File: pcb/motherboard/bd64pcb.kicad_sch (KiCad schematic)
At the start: 224 parts, among them J1 SM04B-SRSS-TB, J2 SM05B-SURS-TF, J3 SM05B-SURS-TF, SW1 SW_Push, U1 ATmega32U4-MU, U2 IS31FL3733-QF, Y1 16MHz

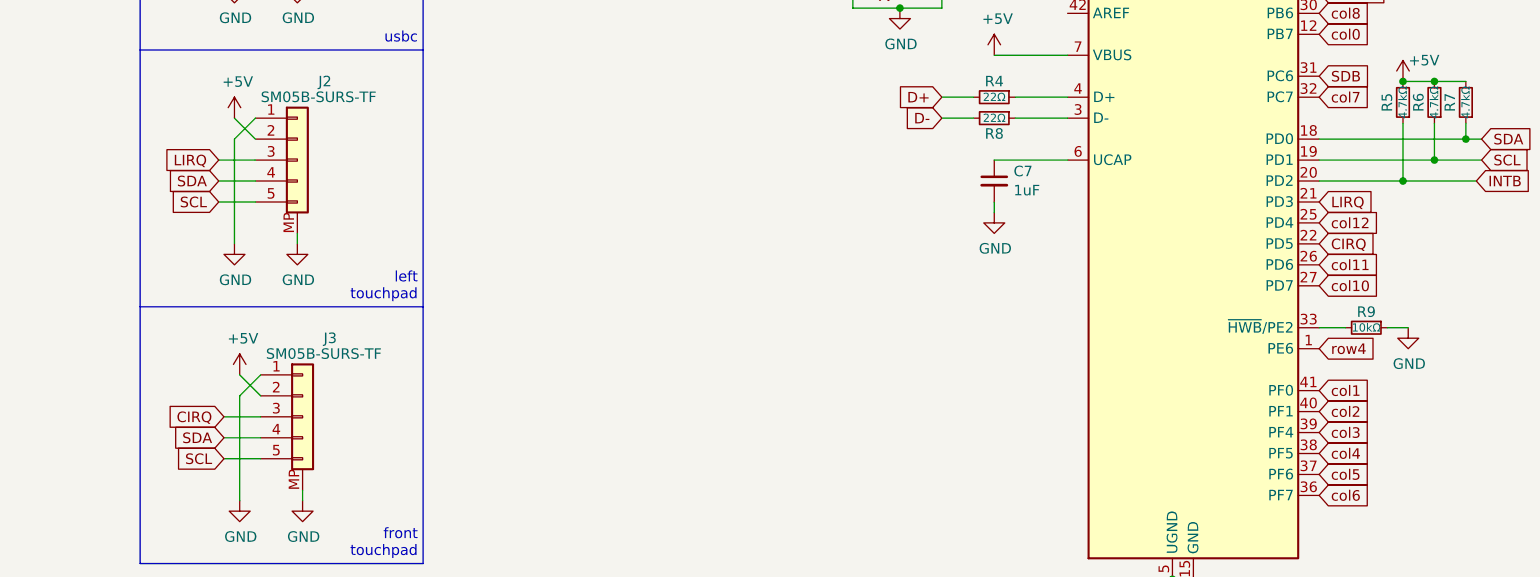
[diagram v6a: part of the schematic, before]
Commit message: IRQ > VIB
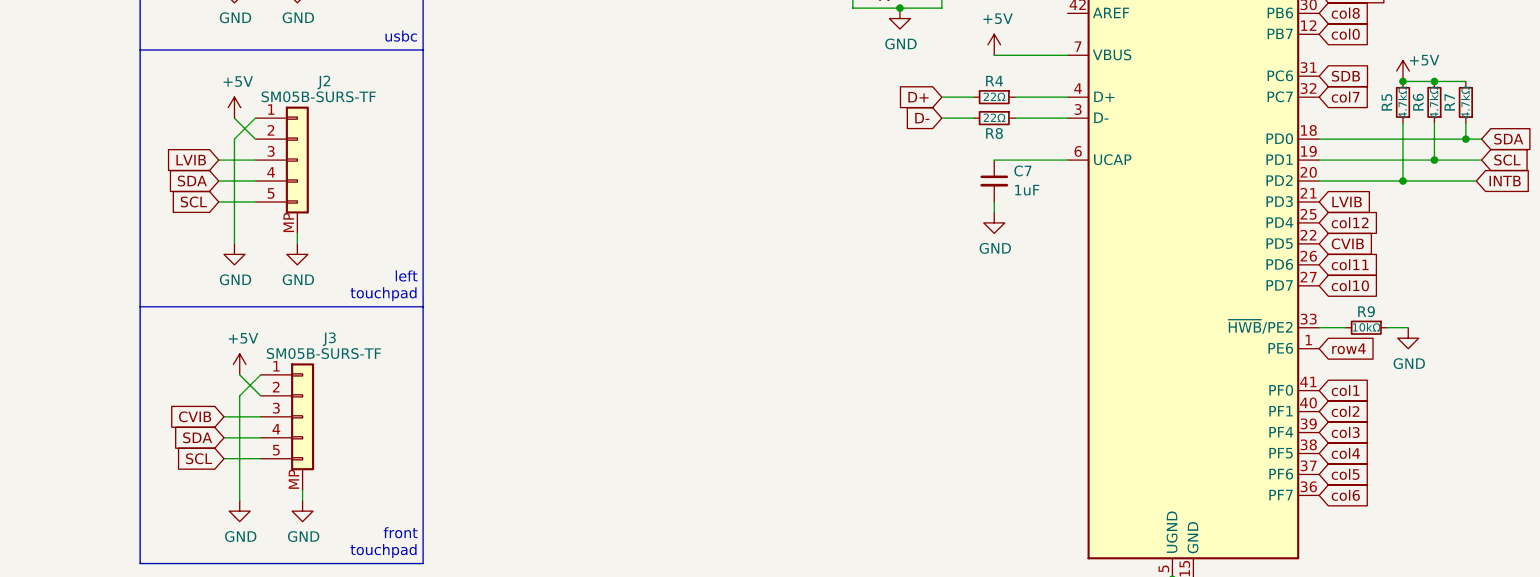
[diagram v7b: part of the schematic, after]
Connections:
- net CIRQ renamed CVIB
- net LIRQ renamed LVIB
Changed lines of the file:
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@@
     )
   )
-  (global_label "CIRQ" (shape input) (at 45.72 105.41 180) (fields_autoplaced)
-    (effects (font (size 1.27 1.27)) (justify right))
-    (property "Intersheet References" "${INTERSHEET_REFS}" (id 0) (at 38.9206 105.3306 0)
+  (global_label "CVIB" (shape input) (at 45.72 105.41 180) (fields_autoplaced)
+    (effects (font (size 1.27 1.27)) (justify right))
+    (property "Intersheet References" "${INTERSHEET_REFS}" (id 0) (at 39.1625 105.3306 0)
       (effects (font (size 1.27 1.27)) (justify right) hide)
     )
@@
     )
   )
-  (global_label "LIRQ" (shape input) (at 45.085 74.295 180) (fields_autoplaced)
-    (effects (font (size 1.27 1.27)) (justify right))
-    (property "Intersheet References" "${INTERSHEET_REFS}" (id 0) (at 38.5275 74.2156 0)
+  (global_label "LVIB" (shape input) (at 45.085 74.295 180) (fields_autoplaced)
+    (effects (font (size 1.27 1.27)) (justify right))
+    (property "Intersheet References" "${INTERSHEET_REFS}" (id 0) (at 38.7694 74.2156 0)
       (effects (font (size 1.27 1.27)) (justify right) hide)
     )
@@
     )
   )
-  (global_label "CIRQ" (shape input) (at 178.435 84.455 0) (fields_autoplaced)
-    (effects (font (size 1.27 1.27)) (justify left))
-    (property "Intersheet References" "${INTERSHEET_REFS}" (id 0) (at 185.2344 84.5344 0)
+  (global_label "CVIB" (shape input) (at 178.435 84.455 0) (fields_autoplaced)
+    (effects (font (size 1.27 1.27)) (justify left))
+    (property "Intersheet References" "${INTERSHEET_REFS}" (id 0) (at 184.9925 84.3756 0)
       (effects (font (size 1.27 1.27)) (justify left) hide)
     )
@@
     )
   )
-  (global_label "LIRQ" (shape input) (at 178.435 79.375 0) (fields_autoplaced)
-    (effects (font (size 1.27 1.27)) (justify left))
-    (property "Intersheet References" "${INTERSHEET_REFS}" (id 0) (at 184.9925 79.4544 0)
+  (global_label "LVIB" (shape input) (at 178.435 79.375 0) (fields_autoplaced)
+    (effects (font (size 1.27 1.27)) (justify left))
+    (property "Intersheet References" "${INTERSHEET_REFS}" (id 0) (at 184.7506 79.2956 0)
       (effects (font (size 1.27 1.27)) (justify left) hide)
     )

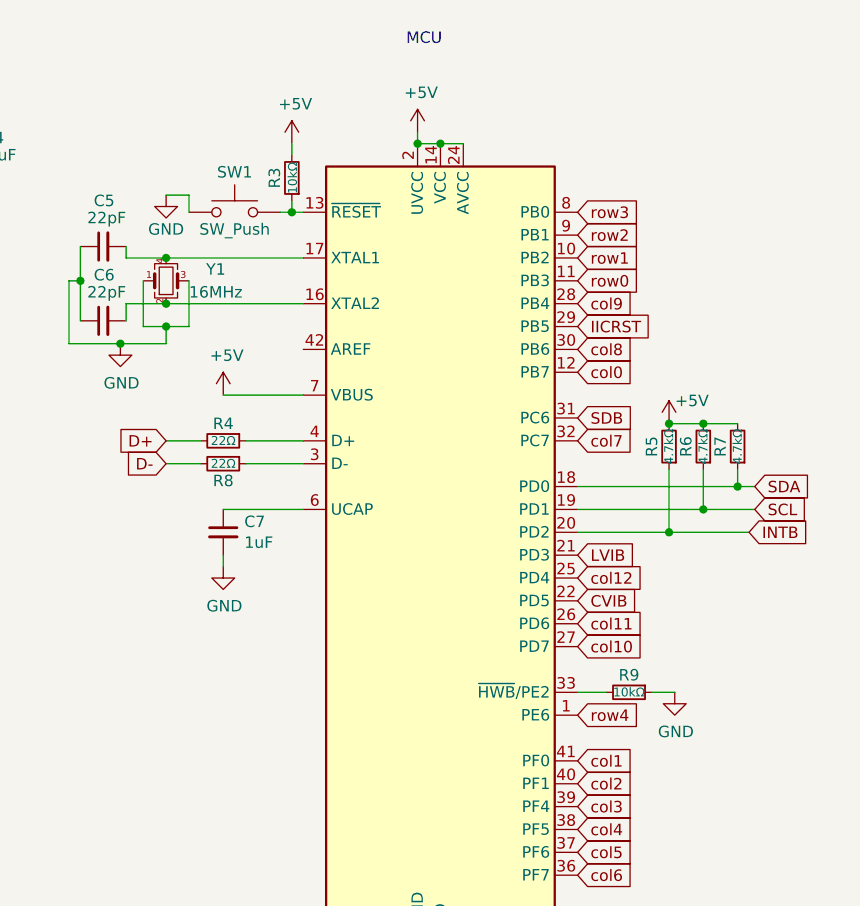
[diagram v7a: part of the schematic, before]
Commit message: HWB to DPDT pushbutton
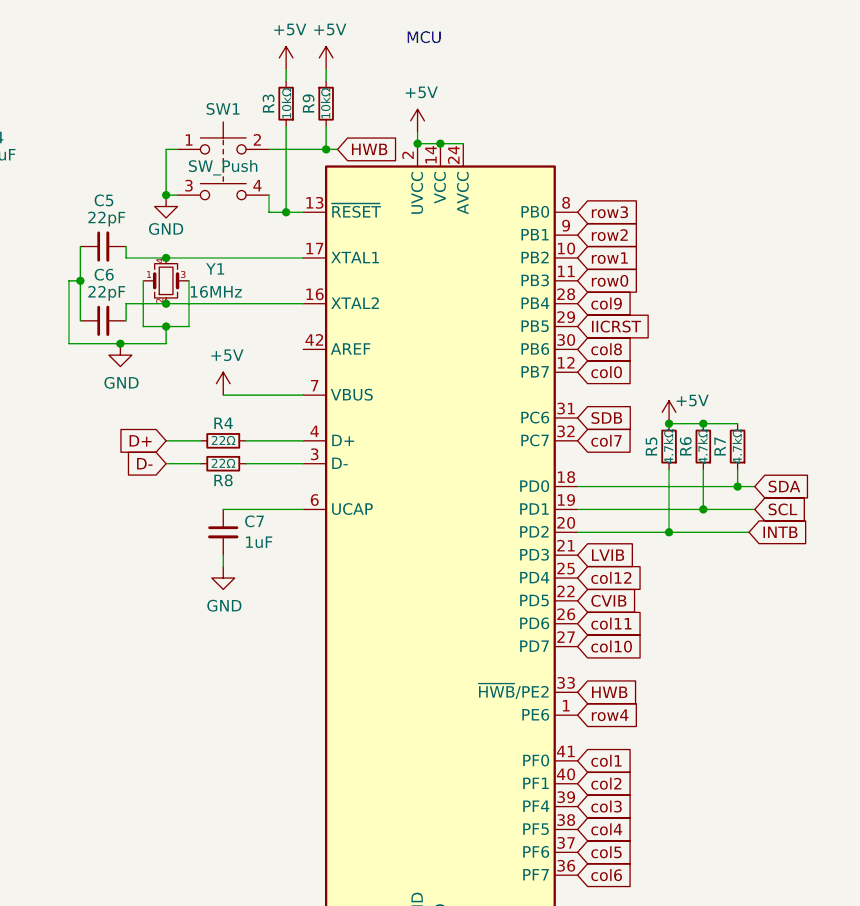
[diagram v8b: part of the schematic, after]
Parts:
- SW1: symbol Switch:SW_Push -> Switch:SW_Push_Dual
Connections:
- net +5V: now also R9.1
- net GND: now also SW1.3; no longer R9.1
- net HWB: now reaches R9.2, U1.33 (~{HWB}/PE2)
- net HWB: now also SW1.2
- net at R3.1, U1.13 (~{RESET}): now also SW1.4; no longer SW1.2
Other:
- moved on the sheet: R3, R9
